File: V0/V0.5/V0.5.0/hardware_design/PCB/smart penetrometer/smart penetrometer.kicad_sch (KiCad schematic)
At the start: 33 parts, among them J1 Screw_Terminal, J2 Conn_01x02, J3 Conn_01x02, J4 Conn_01x07_Female, J5 Conn_02x04, U1 VO615A, U2 ADP7157-3.3, U3 ADS1118IDGS, U4 DS3231M, U5 BME260

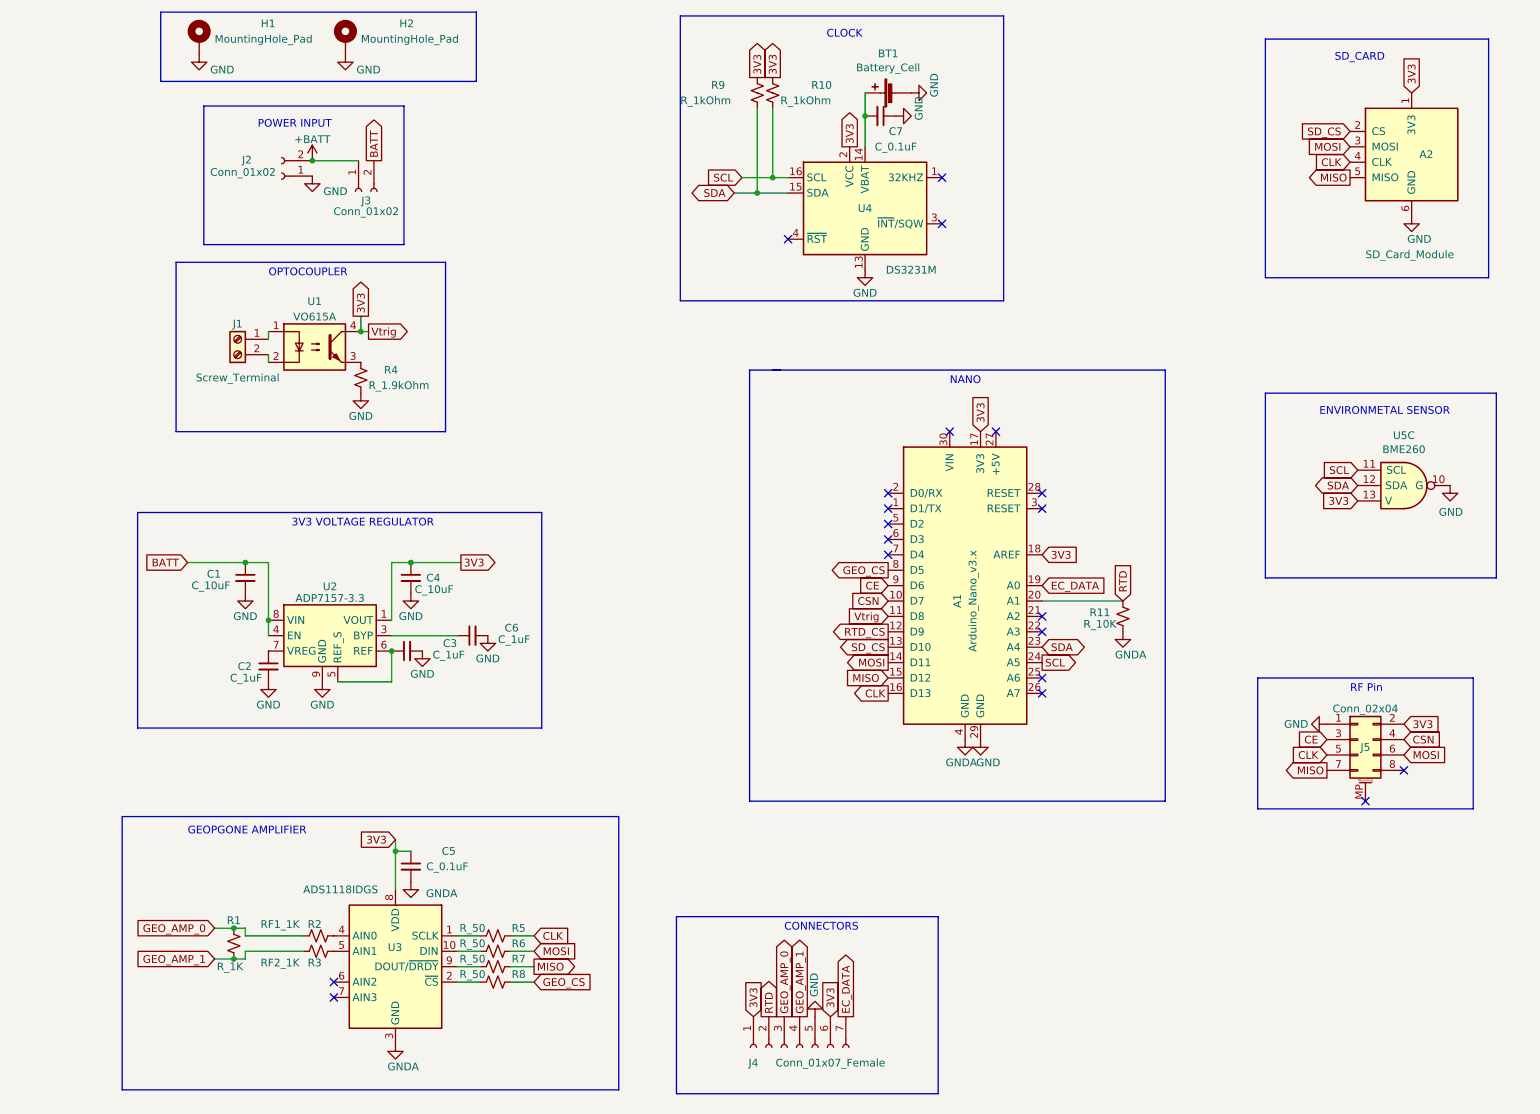
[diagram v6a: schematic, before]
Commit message: reorganized folders
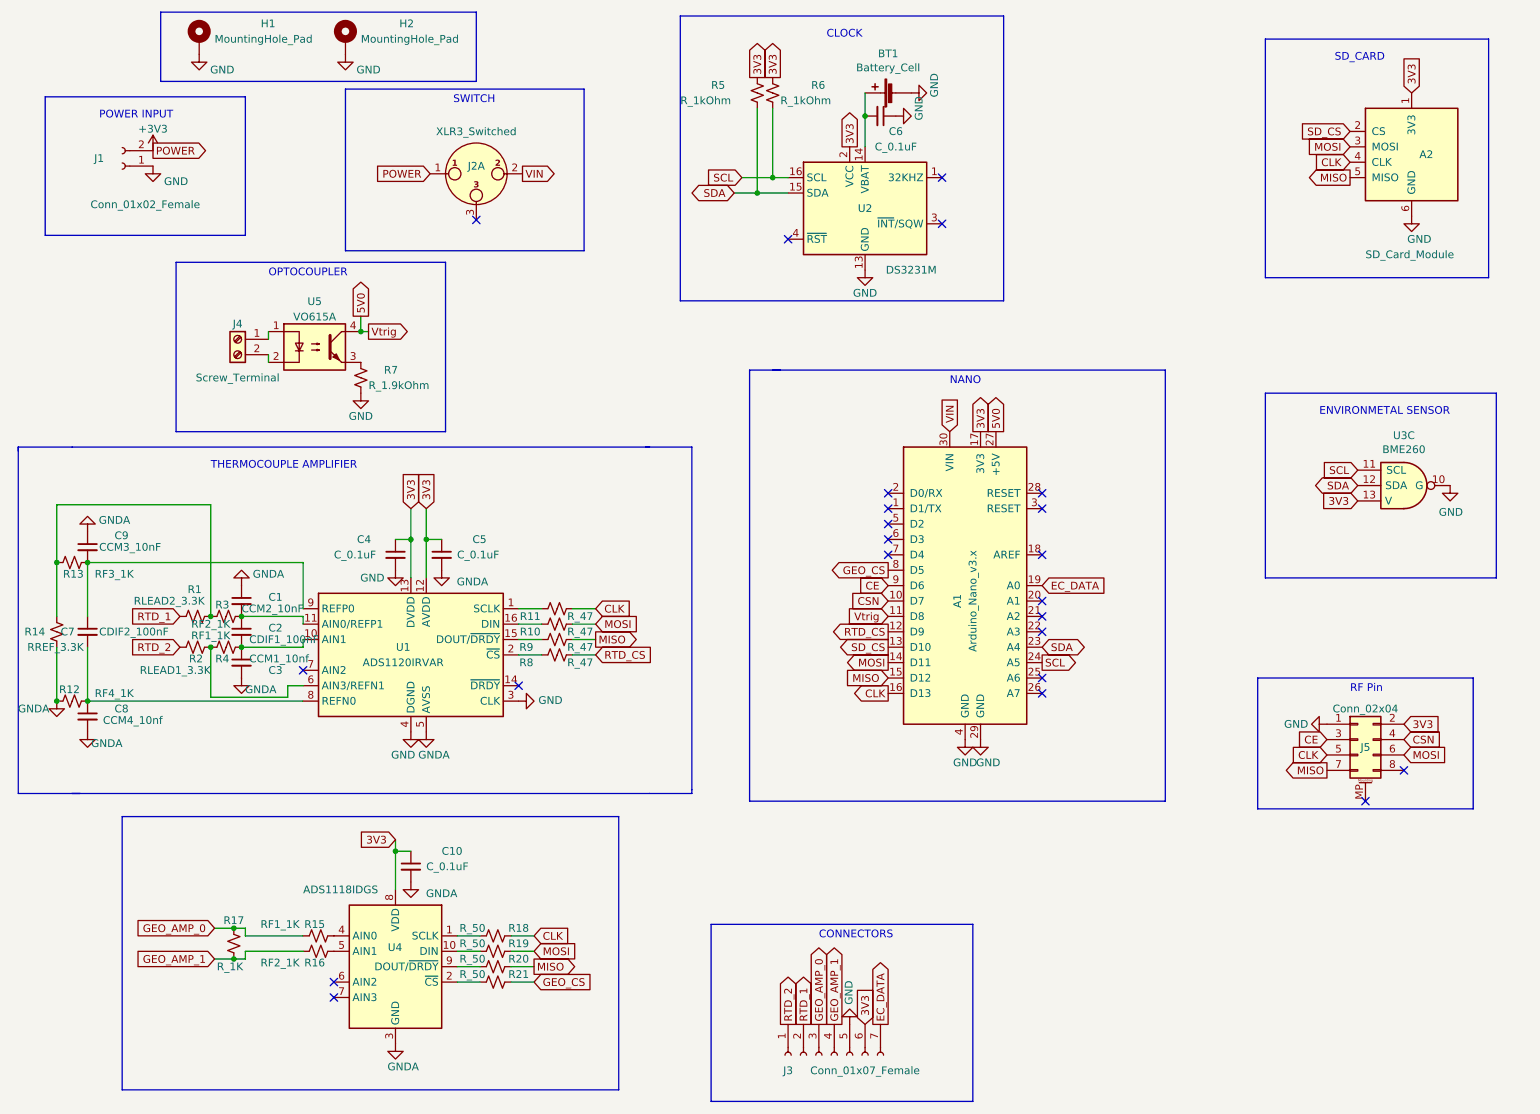
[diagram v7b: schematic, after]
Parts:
- removed C6: C_1uF, Capacitor_SMD:C_1206_3216Metric, symbol Device:C_Small
- removed J3: Conn_01x02, Connector_PinSocket_2.54mm:PinSocket_1x02_P2.54mm_Horizontal, symbol Connector:Conn_01x02_Female
- removed U2: ADP7157-3.3, Package_SO:SOIC-8-1EP_3.9x4.9mm_P1.27mm_EP2.29x3mm, symbol Regulator_Linear:ADP7142ARDZ-3.3
- added C5: C_0.1uF, Capacitor_SMD:C_1206_3216Metric, symbol Device:C_Small
- added C7: CDIF2_100nF, Capacitor_SMD:C_1206_3216Metric, symbol Device:C_Small
- added C8: CCM4_10nf, Capacitor_SMD:C_1206_3216Metric, symbol Device:C_Small
- added C9: CCM3_10nF, Capacitor_SMD:C_1206_3216Metric, symbol Device:C_Small
- added J2: XLR3_Switched, kitest:grounded_switch, symbol Connector:XLR3_Switched
- added R1: RLEAD2_3.3K, Resistor_SMD:R_1206_3216Metric, symbol Device:R_Small_US
- added R10, R8, R9: R_47, Resistor_SMD:R_1206_3216Metric, symbol Device:R_Small_US
- added R12: RF4_1K, Resistor_SMD:R_1206_3216Metric, symbol Device:R_Small_US
- added R13: RF3_1K, Resistor_SMD:R_1206_3216Metric, symbol Device:R_Small_US
- added R14: RREF_3.3K, Resistor_SMD:R_1206_3216Metric, symbol Device:R_Small_US
- added R2: RLEAD1_3.3K, Resistor_SMD:R_1206_3216Metric, symbol Device:R_Small_US
- added R3: RF2_1K, Resistor_SMD:R_1206_3216Metric, symbol Device:R_Small_US
- added R4: RF1_1K, Resistor_SMD:R_1206_3216Metric, symbol Device:R_Small_US
- added U1: ADS1120IRVAR, kitest:ADS1120IPW 16TSSOP, symbol Analog_ADC:ADS1120-PW
- C1: value C_10uF -> CCM2_10nF
- C2: value C_1uF -> CDIF1_100nF
- C3: value C_1uF -> CCM1_10nf
- C4: value C_10uF -> C_0.1uF
- J1: renamed from J2; value Conn_01x02 -> Conn_01x02_Female
- R11: value R_10K -> R_47
- renumbered C5 to C10, C7 to C6, J4 to J3, J1 to J4, R2 to R15, R3 to R16, R1 to R17, R5 to R18, R6 to R19, R7 to R20, R8 to R21, R9 to R5, R10 to R6, R4 to R7, U4 to U2, U5 to U3, U3 to U4, U1 to U5
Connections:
- net BATT is gone; now on net GNDA: C1.1
- net 3V3: now also C5.1, U1.12 (AVDD), U1.13 (DVDD); no longer A1.11 (D8), A1.18 (AREF), J3.1 (Pin_1), U5.4
- net CLK: now also R11.1
- net GND: now also A1.4 (GND), U1.3 (CLK), U1.4 (DGND); no longer C1.2, C2.2, C3.2
- net GNDA: now also C3.2, C5.2, C8.2, C9.1, R12.1, R14.1, U1.5 (AVSS); no longer A1.4 (GND), R11.2
- net MISO: now also R9.1
- net MOSI: now also R10.1
- net RTD_CS: now also R8.1
- net at C2.1: now also C1.2, R3.1, U1.11 (AIN0/REFP1)
- net 5V0: now reaches A1.27 (+5V)
- net 5V0: now also A1.11 (D8), U5.4
- net VIN: now reaches A1.30 (VIN)
- net VIN: now also J2.2
- net at C3.1: now also C2.2, R4.1, U1.10 (AIN1)
- net +BATT renamed +3V3
- net +3V3: now also J2.1
- removed net RTD: A1.20 (A1), J3.2 (Pin_2), R11.1
- new net: C7.2, C8.1, R12.2, U1.8 (REFN0)
- new net: R9.2, U1.15 (DOUT/~{DRDY})
- new net: R1.1, R13.1, R14.2, R3.2
- new net: C7.1, C9.2, R13.2, U1.9 (REFP0)
- new net: R8.2, U1.2 (~{CS})
- new net: R2.2, R4.2, U1.6 (AIN3/REFN1)
- new net: R11.2, U1.1 (SCLK)
- new net: R10.2, U1.16 (DIN)
- new net RTD_1: J3.2 (Pin_2), R1.2
- new net RTD_2: J3.1 (Pin_1), R2.1
- no-connect marks 20 -> 23
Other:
- note added: "SWITCH"
- note added: "THERMOCOUPLE AMPLIFIER"
- note removed: "3V3 VOLTAGE REGULATOR"
- note removed: "GEOPGONE AMPLIFIER"
- moved on the sheet: J1, J3
